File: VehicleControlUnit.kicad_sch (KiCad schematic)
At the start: 0 parts

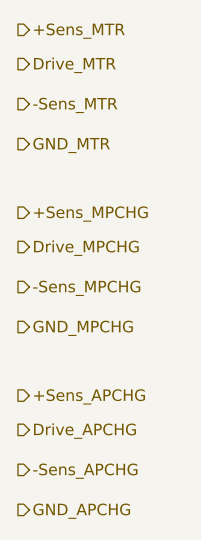
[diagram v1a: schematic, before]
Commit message: new precharge architecture
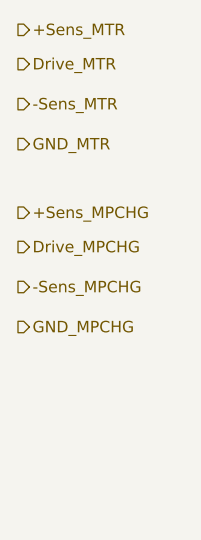
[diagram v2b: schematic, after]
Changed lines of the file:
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@@
-		)
-	)
-	(hierarchical_label "Drive_APCHG"
-		(shape output)
-		(at 140.97 129.54 0)
-		(effects
-			(font
-				(size 1.27 1.27)
-			)
-			(justify left)
 		)
 	)
@@
 		(shape output)
 		(at 140.97 105.41 0)
-		(effects
-			(font
-				(size 1.27 1.27)
-			)
-			(justify left)
-		)
-	)
-	(hierarchical_label "+Sens_APCHG"
-		(shape output)
-		(at 140.97 125.73 0)
-		(effects
-			(font
-				(size 1.27 1.27)
-			)
-			(justify left)
-		)
-	)
-	(hierarchical_label "-Sens_APCHG"
-		(shape output)
-		(at 140.97 133.985 0)
 		(effects
 			(font
@@
 		(effects
 			(font
-				(size 1.27 1.27)
-			)
-			(justify left)
-		)
-	)
-	(hierarchical_label "GND_APCHG"
-		(shape output)
-		(at 140.97 138.43 0)
-		(effects
-			(font

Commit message: done except telemetry
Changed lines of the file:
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@@
+		)
+	)
+	(hierarchical_label "MotorPreSPI"
+		(shape bidirectional)
+		(at 140.97 125.73 0)
+		(effects
+			(font
+				(size 1.27 1.27)
+			)
+			(justify left)
+		)
+	)
+	(hierarchical_label "MotorPreReady"
+		(shape input)
+		(at 140.97 130.175 0)
+		(effects
+			(font
+				(size 1.27 1.27)
+			)
+			(justify left)
 		)
 	)
